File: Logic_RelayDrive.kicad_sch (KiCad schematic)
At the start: 10 parts, among them IC1 TLP3906_TPL,E, J1 Conn_01x04, J7 Conn_01x02, SW1 SW_Nidec_CAS-120A1, U1 SeeeduinoXIAO, U2 AMS1117-3.3, U4 ULN2003A

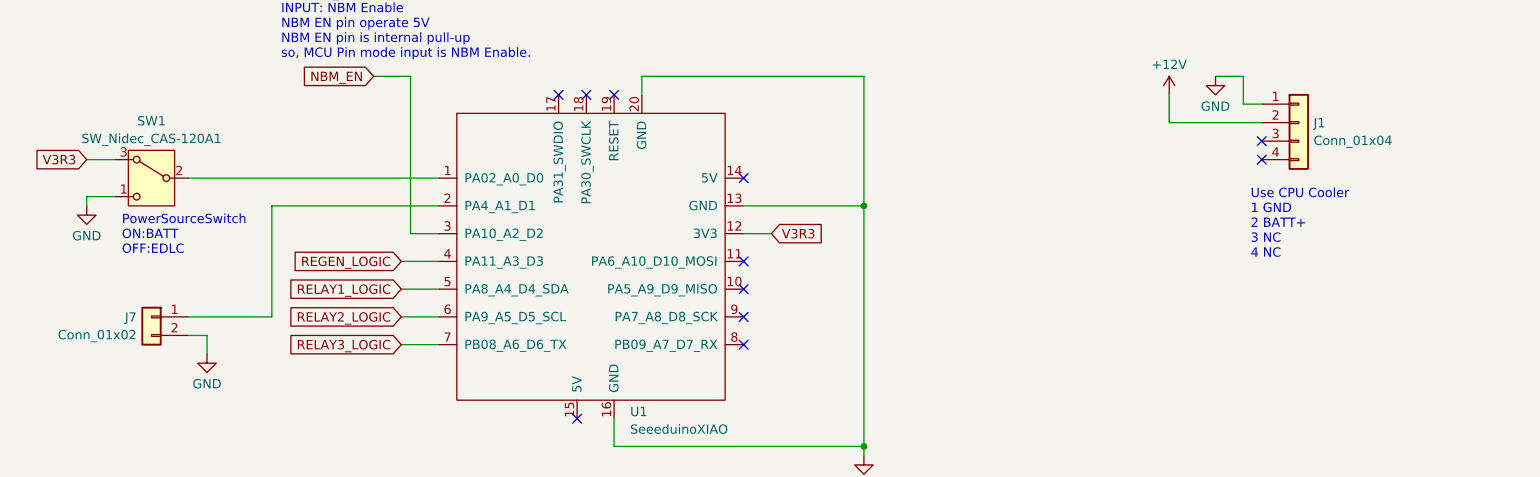
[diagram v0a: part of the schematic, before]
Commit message: Throttle 2pin->3pin and Add C beside of NBM.
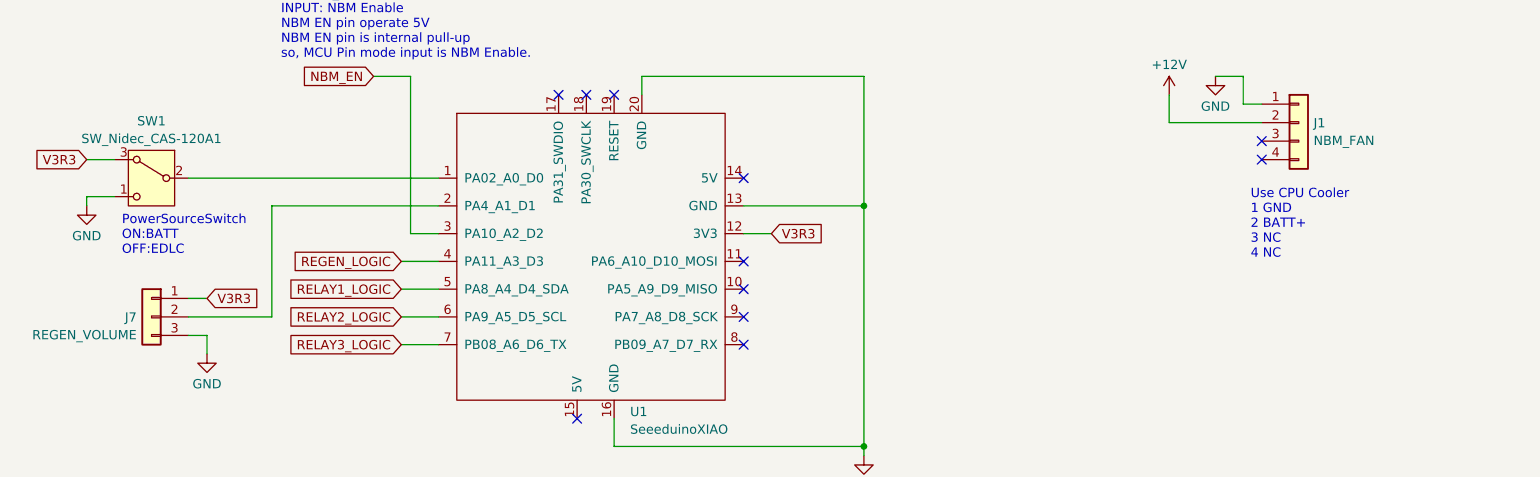
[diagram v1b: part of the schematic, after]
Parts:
- J1: value Conn_01x04 -> NBM_FAN
- J7: value Conn_01x02 -> REGEN_VOLUME; symbol Connector_Generic:Conn_01x02 -> Connector_Generic:Conn_01x03
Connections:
- net GND: now also J7.3 (Pin_3); no longer J7.2 (Pin_2)
- net V3R3: now also J7.1 (Pin_1)
- net at U1.2 (PA4_A1_D1): now also J7.2 (Pin_2); no longer J7.1 (Pin_1)

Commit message: layout done
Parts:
- C1, C2: footprint (none) -> Capacitor_THT:CP_Radial_D5.0mm_P2.00mm
- IC1: footprint SOP254P700X220-4N -> TLP3906:SOP254P700X220-4N
- J1: footprint (none) -> Connector_PinHeader_2.54mm:PinHeader_1x04_P2.54mm_Vertical
- J7: footprint (none) -> Connector_PinHeader_2.54mm:PinHeader_1x03_P2.54mm_Vertical
- R2: footprint (none) -> Resistor_THT:R_Axial_DIN0207_L6.3mm_D2.5mm_P2.54mm_Vertical
- SW1: value SW_Nidec_CAS-120A1 -> BATT-EDLC; footprint Button_Switch_SMD:Nidec_Copal_CAS-120A -> Connector_PinHeader_2.54mm:PinHeader_1x03_P2.54mm_Vertical
- U1: footprint (none) -> SeeduinoXIAO:Seeeduino XIAO-MOUDLE14P-2.54-21X17.8MM
- U4: footprint (none) -> Package_SO:SOIC-16_3.9x9.9mm_P1.27mm
